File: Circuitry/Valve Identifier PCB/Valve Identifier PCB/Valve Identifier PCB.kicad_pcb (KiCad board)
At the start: 2 copper layers, 35.9 x 51.9 mm, 33 parts

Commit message: finalize new pcb design, flipped connector location for the LED breakout board
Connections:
- LED_BOARD_PINS1 pad 09: /GND -> unconnected-(LED_BOARD_PINS1-Pad09)
- LED_BOARD_PINS1 pad 18: unconnected-(LED_BOARD_PINS1-Pad18) -> /GND
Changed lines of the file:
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@@
   (net 32 "/Valve 15")
   (net 33 "/Valve 16")
-  (net 34 "unconnected-(LED_BOARD_PINS1-Pad18)")
+  (net 34 "unconnected-(LED_BOARD_PINS1-Pad09)")
   (footprint "Resistor_THT:R_Axial_DIN0204_L3.6mm_D1.6mm_P2.54mm_Vertical" (layer "F.Cu")
     (at 99.085 92.775)
@@
       (net 25 "/Valve 8") (pinfunction "08") (pintype "passive") (solder_mask_margin 0.102))
     (pad "09" thru_hole circle (at 10.16 1.27) (size 1.53 1.53) (drill 1.02) (layers "*.Cu" "*.Mask")
-      (net 1 "/GND") (pinfunction "09") (pintype "passive") (solder_mask_margin 0.102))
+      (net 34 "unconnected-(LED_BOARD_PINS1-Pad09)") (pinfunction "09") (pintype "passive+no_connect") (solder_mask_margin 0.102))
     (pad "10" thru_hole circle (at -10.16 -1.27) (size 1.53 1.53) (drill 1.02) (layers "*.Cu" "*.Mask")
       (net 26 "/Valve 9") (pinfunction "10") (pintype "passive") (solder_mask_margin 0.102))
@@
       (net 33 "/Valve 16") (pinfunction "17") (pintype "passive") (solder_mask_margin 0.102))
     (pad "18" thru_hole circle (at 10.16 -1.27) (size 1.53 1.53) (drill 1.02) (layers "*.Cu" "*.Mask")
-      (net 34 "unconnected-(LED_BOARD_PINS1-Pad18)") (pinfunction "18") (pintype "passive+no_connect") (solder_mask_margin 0.102))
+      (net 1 "/GND") (pinfunction "18") (pintype "passive") (solder_mask_margin 0.102))
   )
   (gr_line (start 132.425 121.92) (end 96.52 121.92)

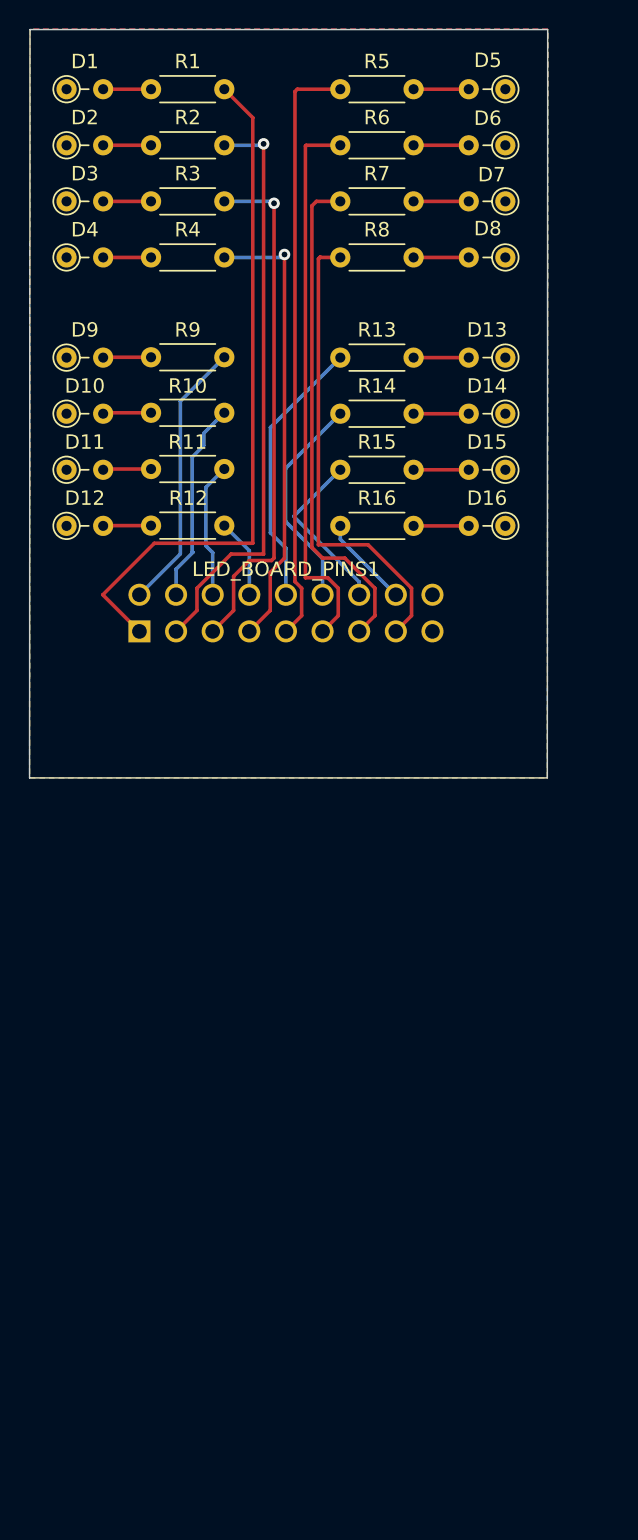
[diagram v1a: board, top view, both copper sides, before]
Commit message: finalize new pcb design, flipped connector location for the LED breakout board
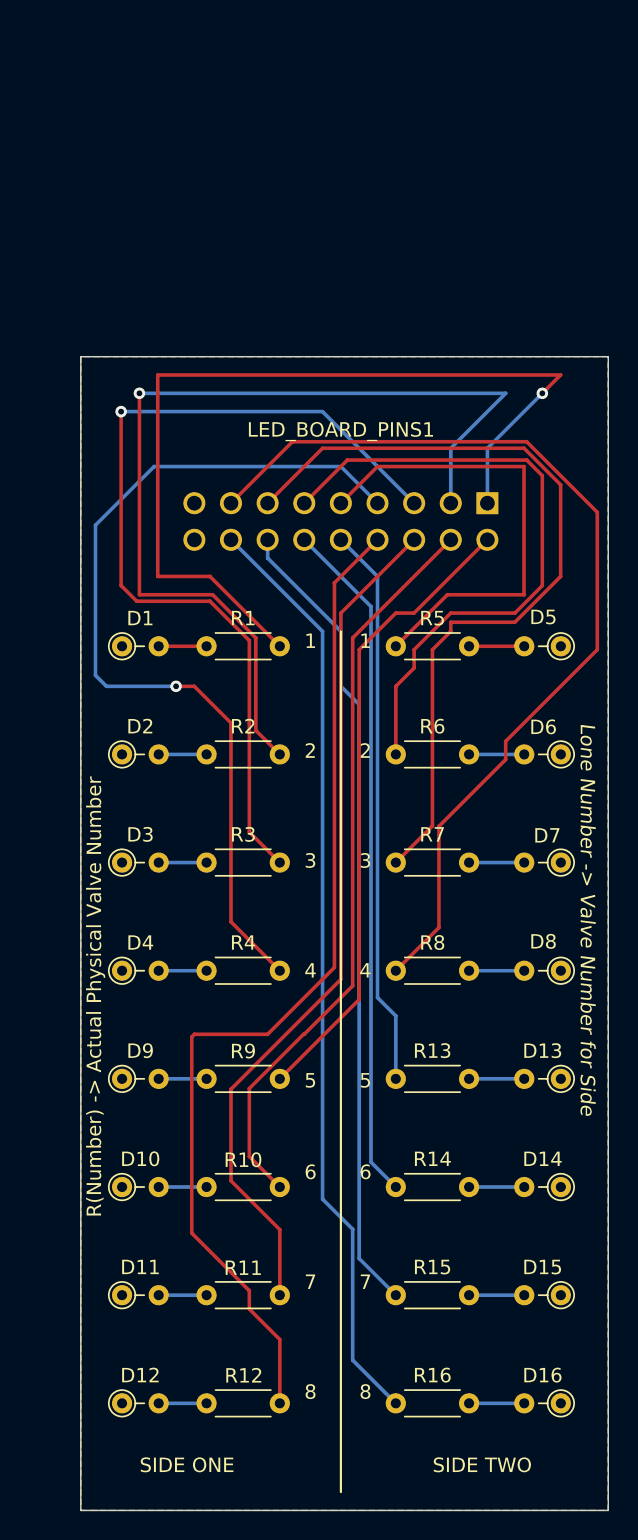
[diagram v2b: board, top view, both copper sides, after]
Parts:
- moved R12 61.0 mm to (113.9, 165.3)
- moved D12 61.0 mm to (102.9, 165.3)
- moved D16 61.0 mm to (133.4, 165.3)
- moved R16 61.0 mm to (121.9, 165.3)
- moved R11 57.4 mm to (113.9, 157.8)
- moved D11 57.4 mm to (102.9, 157.8)
- moved D15 57.4 mm to (133.4, 157.8)
- moved R15 57.4 mm to (121.9, 157.8)
- moved R10 53.8 mm to (113.9, 150.3)
- moved D10 53.8 mm to (102.9, 150.3)
- moved D14 53.8 mm to (133.4, 150.3)
- moved R14 53.8 mm to (121.9, 150.3)
- moved R9 50.2 mm to (113.9, 142.8)
- moved D13 50.2 mm to (133.4, 142.8)
- moved D9 50.2 mm to (102.9, 142.8)
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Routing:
- net /Valve 12: track 5.51 -> 70.7 mm
- net /Valve 16: track 6.37 -> 64.6 mm
- net /Valve 11: track 9.44 -> 59.0 mm
- net /Valve 15: track 11.9 -> 56.1 mm
- net /Valve 10: track 14.0 -> 51.6 mm
- net /Valve 8: track 32.6 -> 66.8 mm
- net /Valve 14: track 15.2 -> 47.5 mm
- net /Valve 4: track 31.4 -> 62.1 mm
- net /Valve 2: track 40.4 -> 66.6 mm
- net /Valve 3: track 35.9 -> 61.8 mm
- net /Valve 9: track 18.9 -> 44.1 mm
- net /Valve 7: track 34.8 -> 56.5 mm
- net /Valve 13: track 18.9 -> 39.0 mm
- net /Valve 1: track 47.8 -> 63.4 mm, vias 0 -> 1
- net /Valve 5: track 41.3 -> 33.0 mm
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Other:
- board size 35.9 x 51.9 mm -> 36.6 x 80 mm
- board text added: "1"
- board text added: "2"
- board text added: "3"
- board text added: "4"
- board text added: "5"
- board text added: "6"
- board text added: "7"
- board text added: "8"
- board text added: "Lone Number -> Valve Number for Side"
- board text added: "R(Number) -> Actual Physical Valve Number"
- board text added: "SIDE ONE"
- board text added: "SIDE TWO"

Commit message: fix breakout board connector orientation
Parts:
- LED_BOARD_PINS1: moved to F.Cu
- turned LED_BOARD_PINS1 to 0 degrees
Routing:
- net /Valve 1: track 63.4 -> 13.6 mm, vias 1 -> 0
- net /Valve 2: track 66.6 -> 20.4 mm, vias 1 -> 0
- net /Valve 3: track 61.8 -> 27.3 mm, vias 1 -> 0
- net /Valve 7: track 56.5 -> 26.9 mm
- net /Valve 8: track 66.8 -> 37.8 mm
- net /Valve 4: track 62.1 -> 34.2 mm, vias 1 -> 0
- net /Valve 6: track 44.3 -> 19.6 mm
- net /Valve 5: track 33.0 -> 11.5 mm
- net /Valve 12: track 70.7 -> 62.9 mm
- net /Valve 11: track 59.0 -> 56.6 mm
- net /Valve 14: track 47.5 -> 49.9 mm
- net /Valve 16: track 64.6 -> 62.3 mm
- net /Valve 15: track 56.1 -> 58.1 mm
